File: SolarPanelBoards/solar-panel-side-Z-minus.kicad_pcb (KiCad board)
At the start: 2 copper layers, 97 x 97.4 mm, 25 parts, among them J1 Conn_01x06, J2 SMA Connector Male, U1 OPT3001DNPT, U2 HHM1589D1

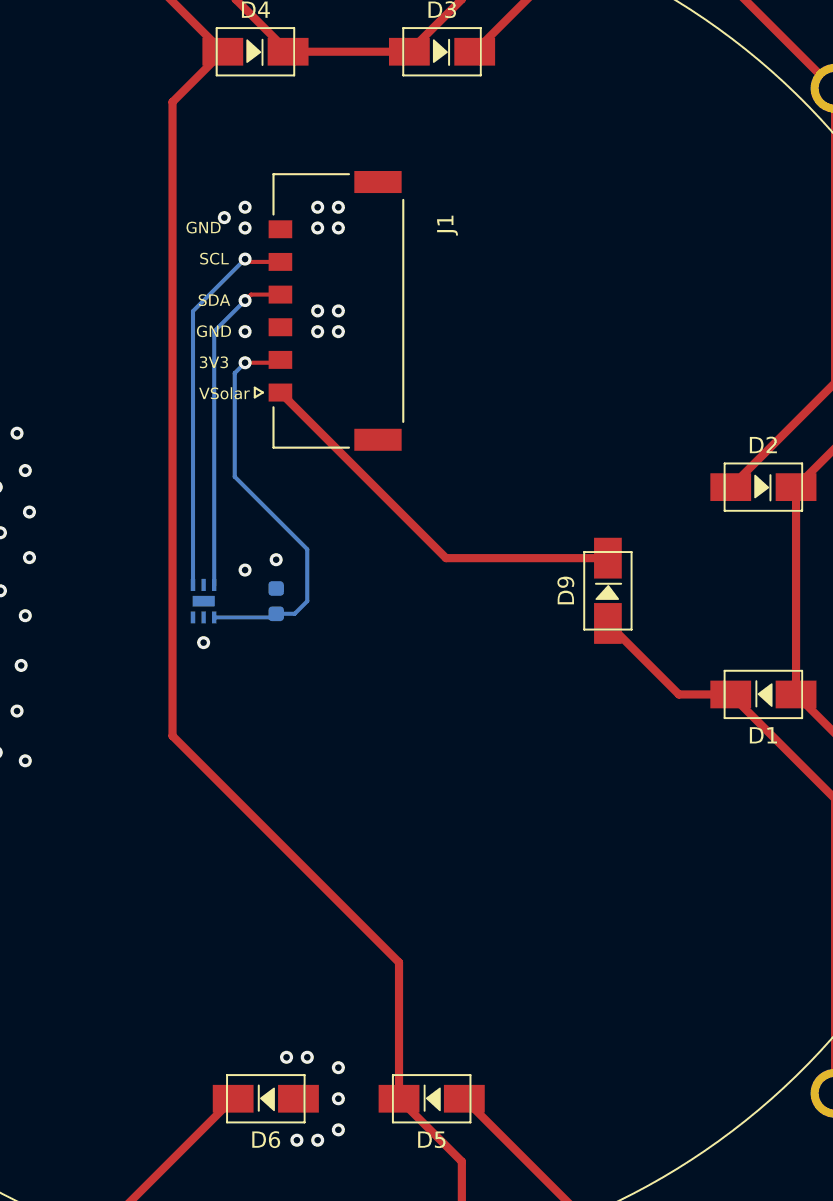
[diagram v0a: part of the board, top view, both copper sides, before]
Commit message: Battery board and side panels ready for CAD check and review, pycubed not finished yet
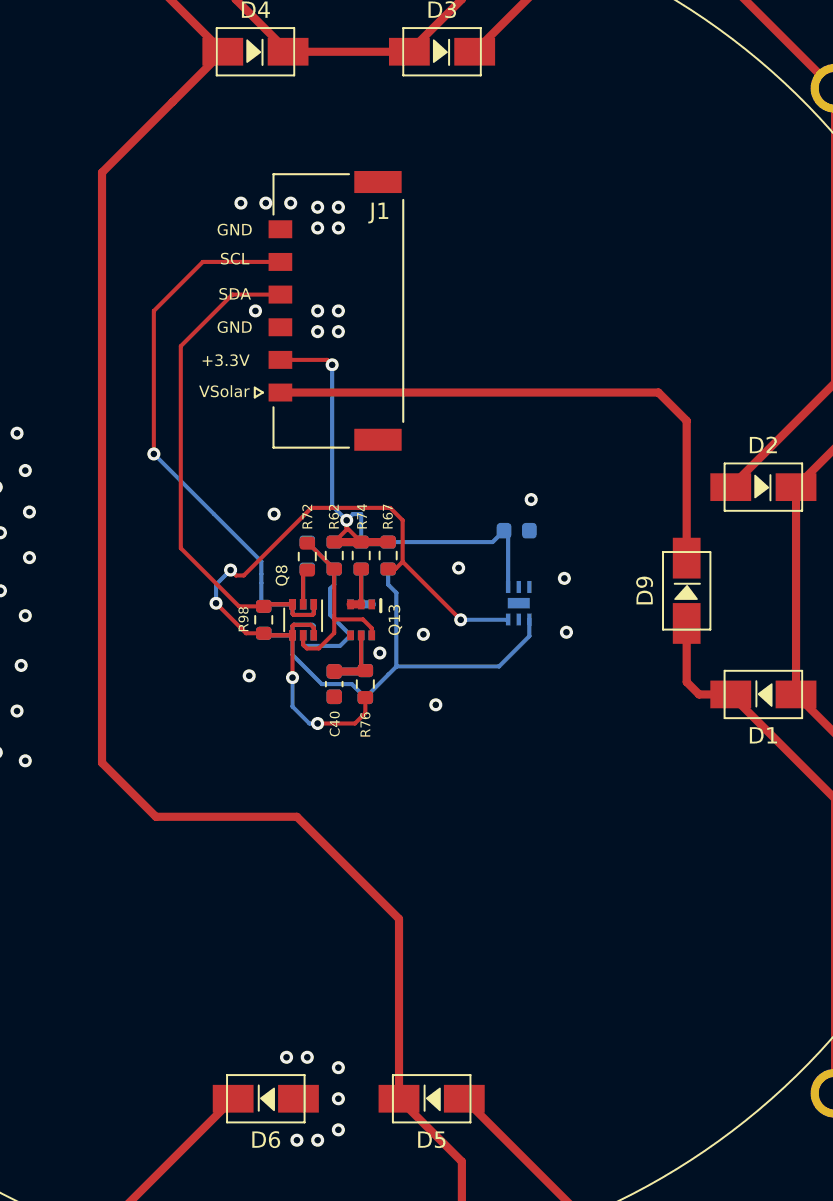
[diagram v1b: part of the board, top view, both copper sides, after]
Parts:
- added C40: 10nF, Capacitor_SMD:C_0603_1608Metric, F.Cu at (149.0, 101.0)
- added C8: 10nF, Capacitor_SMD:C_0603_1608Metric, B.Cu at (149.0, 101.0)
- added Q12: BSS138DWQ-7, sapling:BSS138DWQ-7, B.Cu at (150.6, 97.0)
- added Q13: BSS138DWQ-7, sapling:BSS138DWQ-7, F.Cu at (150.6, 97.0)
- added Q7: MBT2222ADW1T1, Package_TO_SOT_SMD:SOT-363_SC-70-6, B.Cu at (147.1, 97.0)
- added Q8: MBT2222ADW1T1, Package_TO_SOT_SMD:SOT-363_SC-70-6, F.Cu at (147.1, 97.0)
- added R61: 10K, Resistor_SMD:R_0603_1608Metric, B.Cu at (149.0, 93.1)
- added R62: 10K, Resistor_SMD:R_0603_1608Metric, F.Cu at (149.0, 93.1)
- added R66: 10K, Resistor_SMD:R_0603_1608Metric, B.Cu at (152.3, 93.1)
- added R67: 10K, Resistor_SMD:R_0603_1608Metric, F.Cu at (152.3, 93.1)
- added R71: 680, Resistor_SMD:R_0603_1608Metric, B.Cu at (147.3, 93.1)
- added R72: 680, Resistor_SMD:R_0603_1608Metric, F.Cu at (147.3, 93.2)
- added R73: 100K, Resistor_SMD:R_0603_1608Metric, B.Cu at (150.6, 93.1)
- added R74: 100K, Resistor_SMD:R_0603_1608Metric, F.Cu at (150.6, 93.1)
- added R75: 200K, Resistor_SMD:R_0603_1608Metric, B.Cu at (150.9, 101.0)
- added R76: 200K, Resistor_SMD:R_0603_1608Metric, F.Cu at (150.9, 101.0)
- added R97: 0, Resistor_SMD:R_0603_1608Metric, B.Cu at (144.7, 97.0)
- added R98: 0, Resistor_SMD:R_0603_1608Metric, F.Cu at (144.7, 97.0)
- moved U1 19.3 mm to (160.3, 96.0), turned to 270 degrees
- moved C1 15.4 mm to (160.1, 91.6), turned to 0 degrees
- moved D9 4.83 mm to (170.6, 95.2)
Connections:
- U1 pad 4: SCL -> SCL_SUN
- U1 pad 6: SDA -> SDA_SUN
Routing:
- net SDA_SUN: track 0.00 -> 45.1 mm, vias 0 -> 5
- net SCL_SUN: track 0.00 -> 29.9 mm
- net Net-(Q13-Pad6): track 0.00 -> 12.2 mm
- net +3V3: track 25.1 -> 37.1 mm, vias 1 -> 2
- net Net-(Q12-Pad6): track 0.00 -> 10.8 mm
- net SCL: track 23.5 -> 34.2 mm
- net SDA: track 20.5 -> 30.7 mm, vias 1 -> 0
- net VSOLAR: track 24.3 -> 34.0 mm
- net Net-(D4-Pad2): track 100.0 -> 108.6 mm
- net Net-(C8-Pad1): track 0.00 -> 4.19 mm
- net Net-(C40-Pad1): track 0.00 -> 4.19 mm
- net Net-(Q13-Pad2): track 0.00 -> 2.81 mm
- net Net-(Q12-Pad2): track 0.00 -> 2.81 mm
- net Net-(D1-Pad1): track 36.4 -> 33.7 mm
- net Net-(Q7-Pad2): track 0.00 -> 2.27 mm
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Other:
- board text added: "+3.3V"
- board text removed: "."
- board text removed: "3V3"
- board text removed: "Sapling Rev. 1 SSI Satellites"

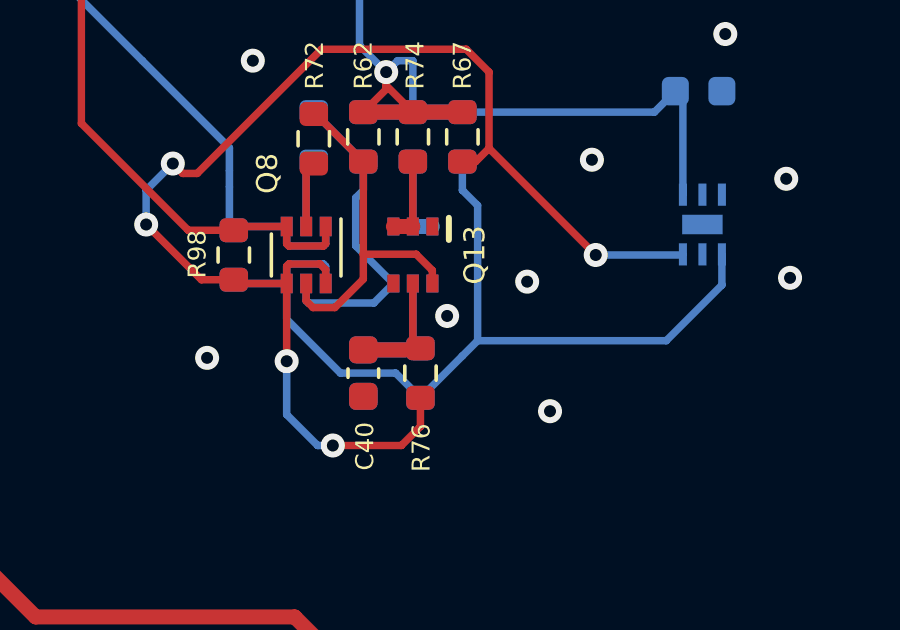
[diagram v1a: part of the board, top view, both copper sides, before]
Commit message: side panels ready except for RF trace width
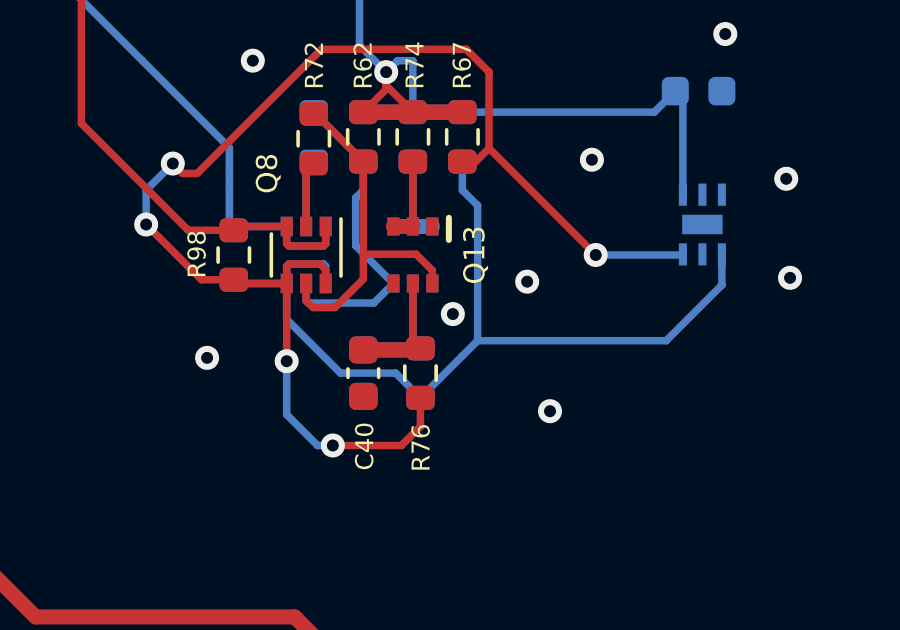
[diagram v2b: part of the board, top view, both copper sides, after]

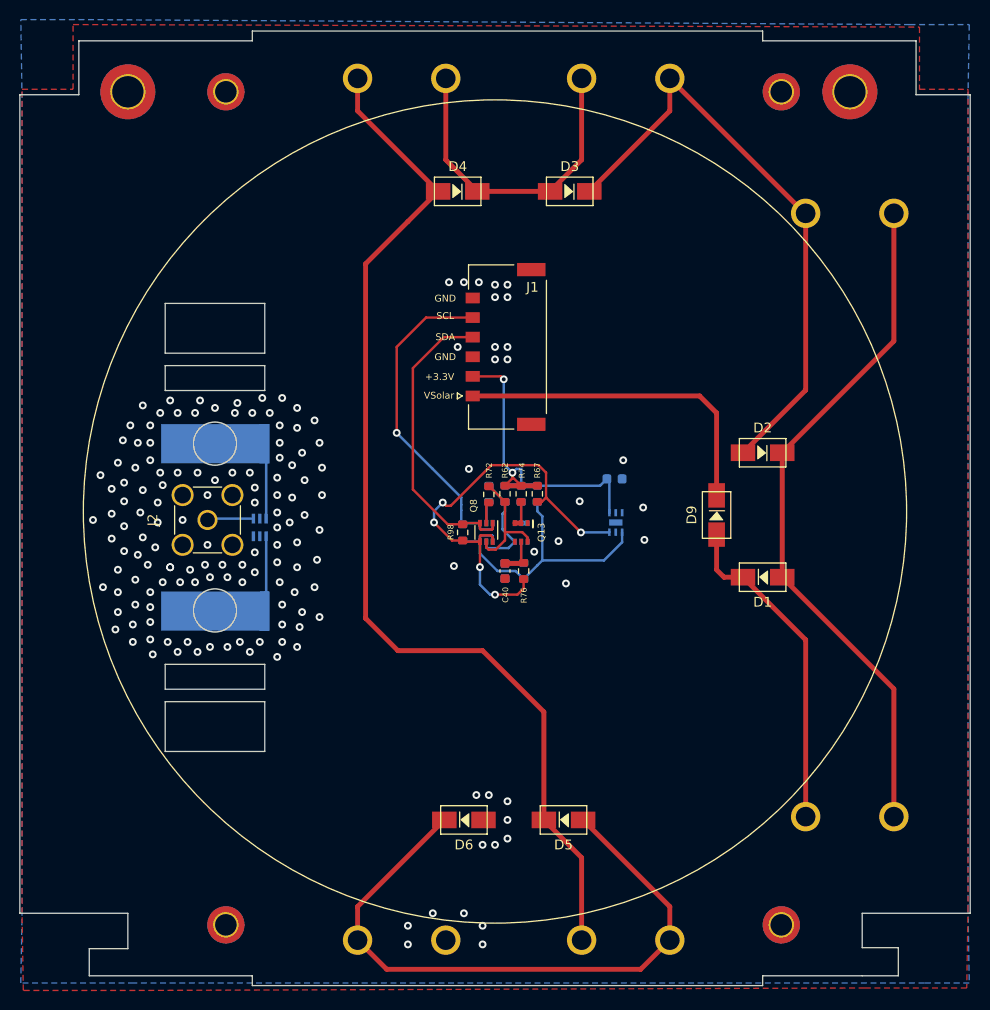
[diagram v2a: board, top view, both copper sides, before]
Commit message: Changed outline of minus z plates to accommodate switch
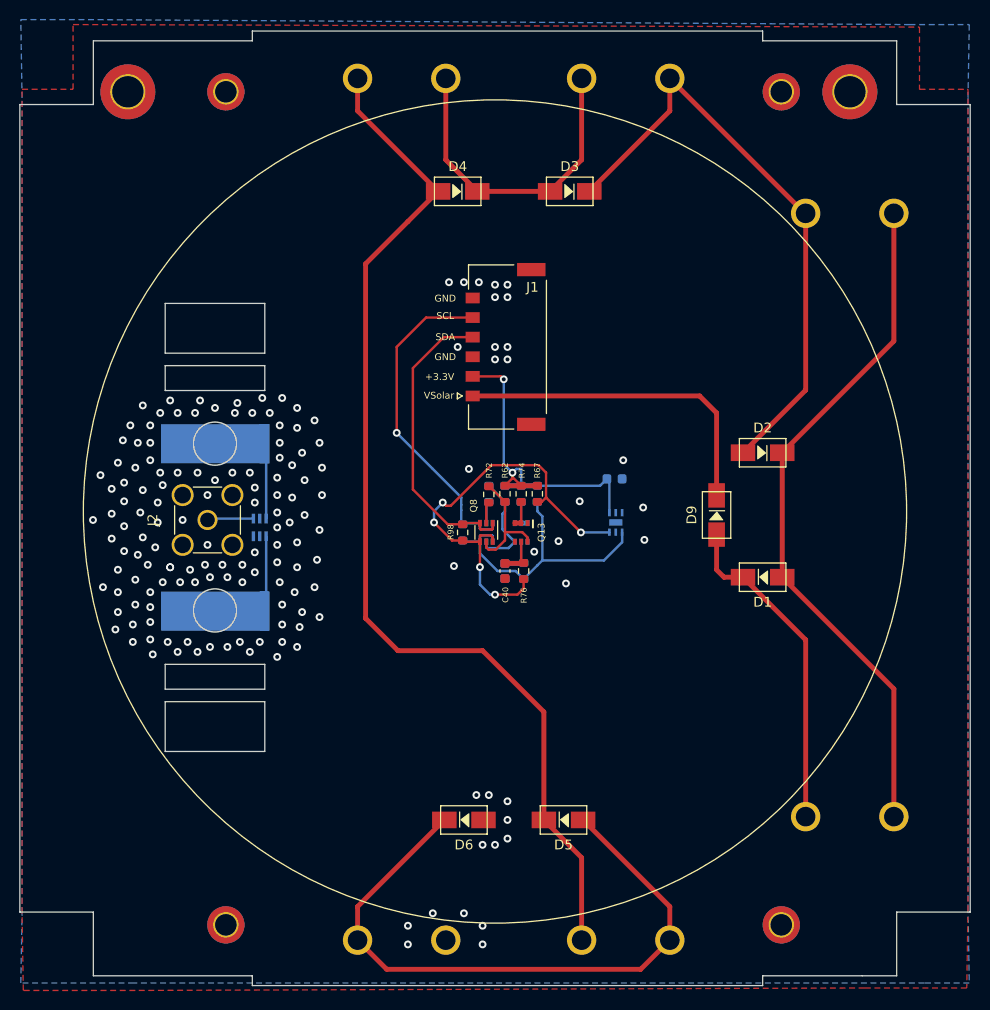
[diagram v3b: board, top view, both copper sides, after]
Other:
- outline, holes or cut-outs redrawn
- net class Default removed
